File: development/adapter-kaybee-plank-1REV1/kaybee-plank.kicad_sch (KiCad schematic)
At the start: 27 parts, among them J1 Mini-DIN-6, J2 Conn_01x10, J3 Conn_01x10, J4 Mini-DIN-6, J5 USB_A, J7 TYPE-C-31-M-12, J8 Conn_01x02_Pin, J9 Conn_01x02_Pin, Q401 BCM857BS-7-F, Q402 BC2301T 2.8A, SW1 SW_SPDT

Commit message: kaybee production package
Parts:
- D401: szlcsc_partnum (none) -> C2828426
- Q401: szlcsc_partnum (none) -> C105896
- Q402: szlcsc_partnum (none) -> C21714127
- R408: value 66K -> 68K; szlcsc_partnum (none) -> C17801
- R410: szlcsc_partnum (none) -> C17414
- R412: szlcsc_partnum (none) -> C149504
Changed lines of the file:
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@@
+			)
+		)
+		(property "szlcsc_partnum" "C2828426"
+			(at 200.66 105.41 0)
+			(effects
+				(font
+					(size 1.27 1.27)
+				)
 			)
 		)
@@
 				)
 				(hide yes)
+			)
+		)
+		(property "szlcsc_partnum" "C17414"
+			(at 204.47 109.22 0)
+			(effects
+				(font
+					(size 1.27 1.27)
+				)
 			)
 		)
@@
 			)
 		)
-		(property "Value" "66K"
+		(property "Value" "68K"
 			(at 198.12 118.364 0)
 			(effects
@@
 				)
 				(hide yes)
+			)
+		)
+		(property "szlcsc_partnum" "C17801"
+			(at 193.04 116.84 0)
+			(effects
+				(font
+					(size 1.27 1.27)
+				)
 			)
 		)
@@
 			)
 		)
+		(property "szlcsc_partnum" "C105896"
+			(at 195.58 109.22 0)
+			(effects
+				(font
+					(size 1.27 1.27)
+				)
+			)
+		)
 		(pin "1"
 		)
@@
 			)
 		)
+		(property "szlcsc_partnum" "C105896"
+			(at 213.36 109.22 0)
+			(effects
+				(font
+					(size 1.27 1.27)
+				)
+			)
+		)
 		(pin "1"
 		)
@@
 				)
 				(hide yes)
+			)
+		)
+		(property "szlcsc_partnum" "C21714127"
+			(at 204.47 100.33 0)
+			(effects
+				(font
+					(size 1.27 1.27)
+				)
 			)
 		)
@@
 			)
 		)
+		(property "szlcsc_partnum" "C149504"
+			(at 215.9 116.84 0)
+			(effects
+				(font
+					(size 1.27 1.27)
+				)
+			)
+		)

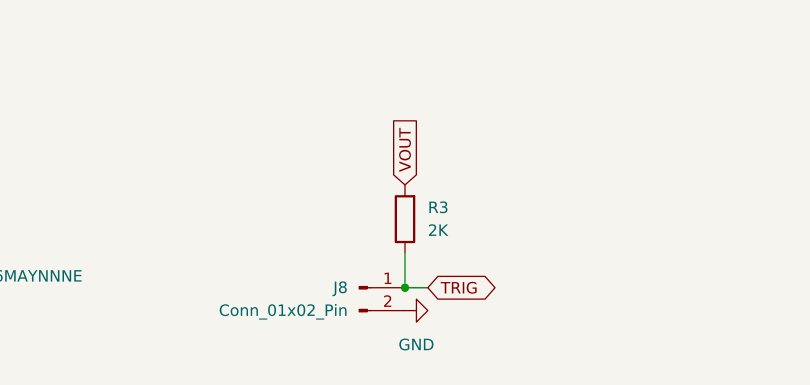
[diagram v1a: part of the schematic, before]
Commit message: kaybee plank - change pull-up resistor supply source
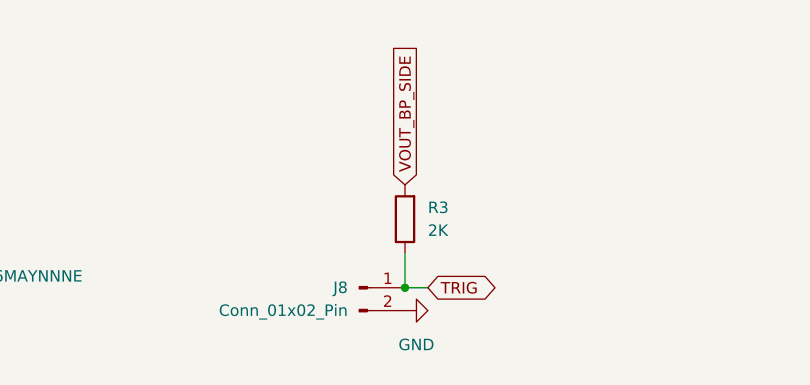
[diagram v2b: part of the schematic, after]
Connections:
- net VOUT: no longer R3.2
- net VOUT_BP_SIDE: now also R3.2
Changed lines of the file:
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@@
 		)
 	)
-	(global_label "VOUT"
+	(global_label "VOUT_BP_SIDE"
 		(shape input)
 		(at 167.64 33.02 90)
@@
 		)
 		(property "Intersheetrefs" "${INTERSHEET_REFS}"
-			(at 167.64 25.3176 90)
+			(at 167.64 16.6091 90)
 			(effects
 				(font
